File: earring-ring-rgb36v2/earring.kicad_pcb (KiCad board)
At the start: 2 copper layers, 75 x 92.5 mm, 65 parts, among them J1 Conn_01x05, Q1 AO3401A, Q2 Q_Photo_NPN_EC, SW1 SW_Push, U2 STM32L031G6Ux, Y1 Crystal

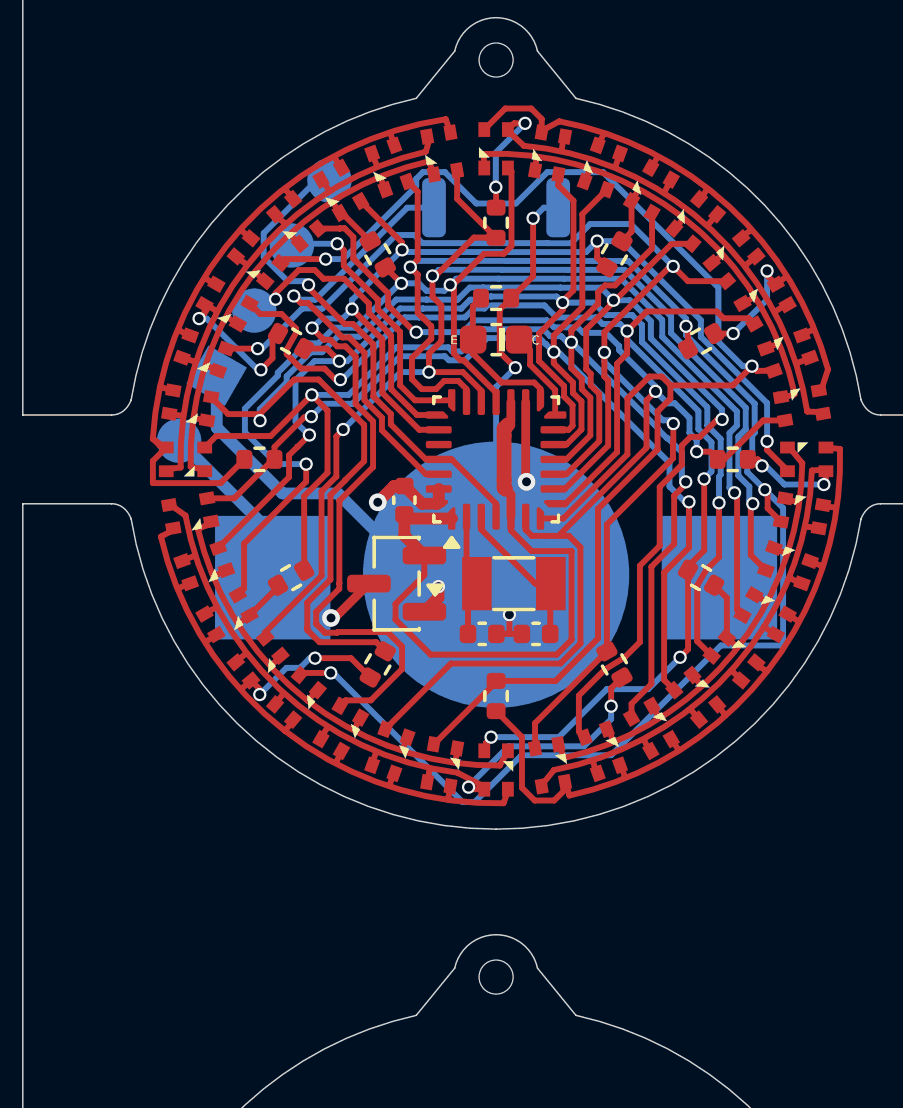
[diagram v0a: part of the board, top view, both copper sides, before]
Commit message: earring-ring-rgb36v2: add microphone
This also required reworking the PCB a little.
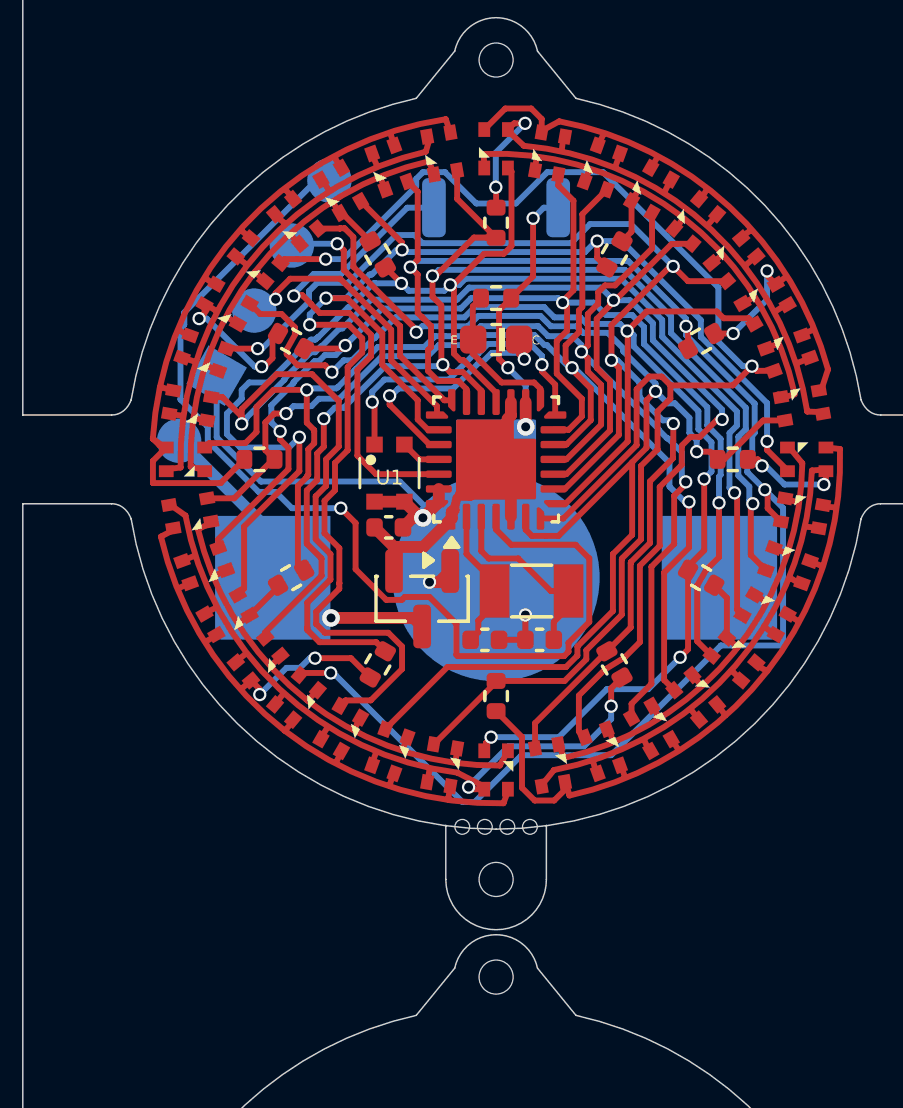
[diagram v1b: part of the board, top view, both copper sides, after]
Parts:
- added REF**: ToolingHoleWithMouseBytes, Custom:ToolingHoleWithMouseBytes, F.Cu at (0.00, 14.2)
- added U1: GMA2718H09-F42-4P, Custom:GMA2718H09-F42-4P, F.Cu at (-3.60, 0.47)
- moved C1 1.06 mm to (-3.63, 2.30), turned to 0 degrees
- moved Q1 1.00 mm to (-2.50, 4.71), turned to -90 degrees
- moved Y1 0.65 mm to (1.20, 4.45)
- moved C3 0.23 mm to (1.47, 6.10)
- moved C2 0.22 mm to (-0.38, 6.10)
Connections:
- U2 pad 14: PHOTO_VCC -> MIC_SENSE
- U2 pad 24: unconnected-(U2-PB3-Pad24) -> PHOTO_VCC
- U2 pad 25: NRST -> MIC_VCC
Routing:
- net NRST: track 16.8 -> 35.9 mm
- net VCC: track 22.4 -> 8.89 mm
- net MIC_SENSE: track 0.00 -> 10.6 mm, vias 0 -> 2
- net GND: track 43.2 -> 34.2 mm
- net PHOTO_VCC: track 3.05 -> 8.57 mm, vias 0 -> 2
- net A12: track 41.1 -> 44.1 mm
- net Net-(U2-PB7): track 14.7 -> 16.5 mm
- net A1: track 49.5 -> 51.3 mm
- net A4: track 47.5 -> 49.3 mm
- net VBAT: track 9.99 -> 11.5 mm
- net MIC_VCC: track 0.00 -> 1.37 mm
- net Net-(U2-PC15): track 5.25 -> 6.53 mm
- net A2: track 55.4 -> 54.3 mm
- net A6: track 38.9 -> 39.7 mm
- net A3: track 42.3 -> 43.1 mm
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
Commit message: earring-ring-rgb36v2: switch to 10k resistor for light sensing
Based on some very rough measurements and calculations, I think this
will end up as ~2V input voltage on the ADC on a bright 400 nits
display.

This is also the version that was sent to JLCPCB as a test production.
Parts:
- R13: value 1k -> 10k
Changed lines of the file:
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@@
 			)
 		)
-		(property "Value" "1k"
+		(property "Value" "10k"
 			(at 0 1.17 0)
 			(layer "F.Fab")
@@
 			)
 		)
-		(property "LCSC" "C11702"
+		(property "LCSC" "C25756"
 			(at 0 0 0)
 			(unlocked yes)

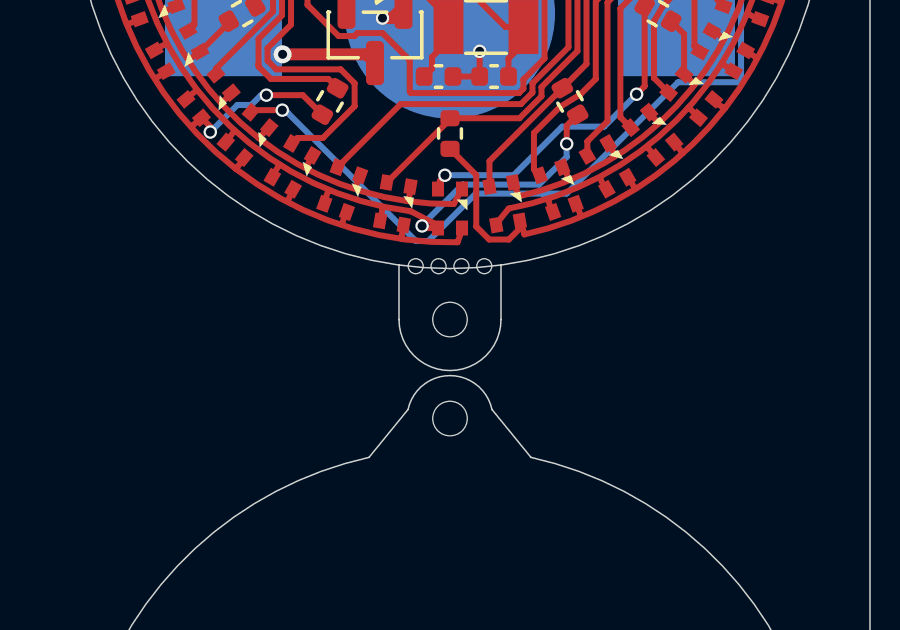
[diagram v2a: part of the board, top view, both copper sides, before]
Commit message: earring-ring-rgb36v2: add 3D model for the microphone
Also remove the tooling hole at the bottom, they were messing with the
3D view.
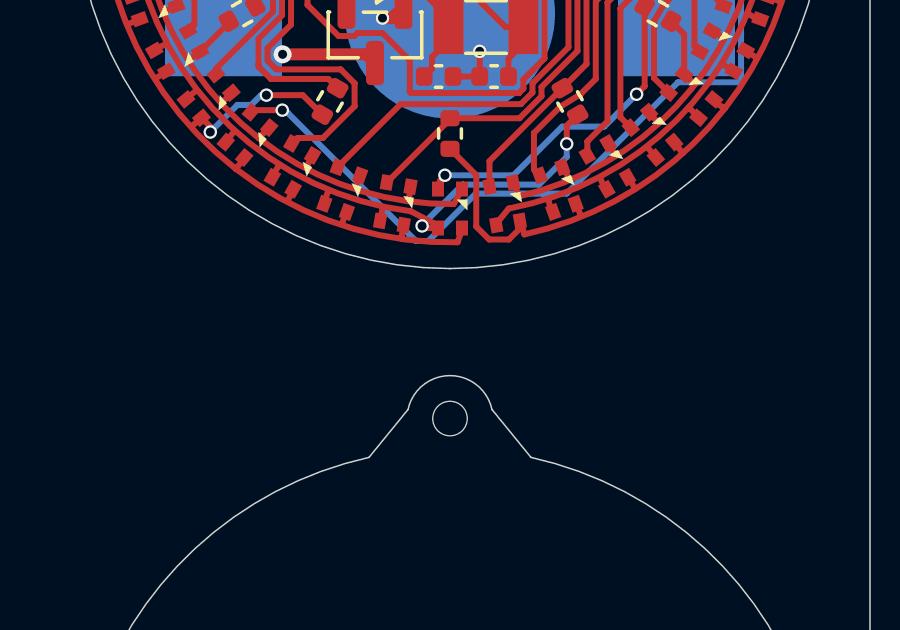
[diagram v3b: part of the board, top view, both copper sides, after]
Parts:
- removed REF**: ToolingHoleWithMouseBytes, Custom:ToolingHoleWithMouseBytes
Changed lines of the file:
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@@
 		)
 		(embedded_fonts no)
+		(model "../../../third_party/lcsc/C5142165.step"
+			(offset
+				(xyz 0 0 0.5)
+			)
+			(scale
+				(xyz 1 1 1)
+			)
+			(rotate
+				(xyz -0 -0 -0)
+			)
+		)
 	)
 	(footprint "Custom:NH-Z1415RGBA-SG"
@@
 		)
 	)
-	(footprint "Custom:ToolingHoleWithMouseBytes"
-		(layer "F.Cu")
-		(at 0 14.2)
-		(property "Reference" "REF**"
-			(at 0 -5.1 0)
-			(unlocked yes)
-			(layer "F.SilkS")
-			(hide yes)
-			(effects
-				(font
-					(size 1 1)
-					(thickness 0.1)
-				)
-			)
-		)
-		(property "Value" "ToolingHoleWithMouseBytes"
-			(at 0 -3.6 0)
-			(unlocked yes)
-			(layer "F.Fab")
-			(hide yes)
-			(effects
-				(font
-					(size 1 1)
-					(thickness 0.15)
-				)
-			)
-		)
-		(property "Datasheet" ""
-			(at 0 0 0)
-			(unlocked yes)
-			(layer "F.Fab")
-			(hide yes)
-			(effects
-				(font
-					(size 1 1)
-					(thickness 0.15)
-				)
-			)
-		)
-		(property "Description" ""
-			(at 0 0 0)
-			(unlocked yes)
-			(layer "F.Fab")
-			(hide yes)
-			(effects
-				(font
-					(size 1 1)
-					(thickness 0.15)
-				)
-			)
-		)
-		(attr through_hole board_only dnp)
-		(fp_line
-			(start -1.7 0)
-			(end -1.7 -1.83)
-			(stroke
-				(width 0.05)
-				(type default)
-			)
-			(layer "Edge.Cuts")
-		)
-		(fp_line
-			(start 1.7 0)
-			(end 1.7 -1.83)
-			(stroke
-				(width 0.05)
-				(type default)
-			)
-			(layer "Edge.Cuts")
-		)
-		(fp_arc
-			(start 1.7 0)
-			(mid 0 1.7)
-			(end -1.7 0)
-			(stroke
-				(width 0.05)
-				(type default)
-			)
-			(layer "Edge.Cuts")
-		)
-		(pad "" np_thru_hole circle
-			(at -1.143 -1.778)
-			(size 0.5 0.5)
-			(drill 0.5)
-			(layers "*.Mask")
-		)
-		(pad "" np_thru_hole circle
-			(at -0.381 -1.778)
-			(size 0.5 0.5)
-			(drill 0.5)
-			(layers "*.Mask")
-		)
-		(pad "" np_thru_hole circle
-			(at 0 0)
-			(size 1.152 1.152)
-			(drill 1.152)
-			(layers "*.Mask")
-			(solder_mask_margin 0.148)
-			(clearance 0.248)
-		)
-		(pad "" np_thru_hole circle
-			(at 0.381 -1.778)
-			(size 0.5 0.5)
-			(drill 0.5)
-			(layers "*.Mask")
-		)
-		(pad "" np_thru_hole circle
-			(at 1.143 -1.778)
-			(size 0.5 0.5)
-			(drill 0.5)
-			(layers "*.Mask")
-		)
-		(embedded_fonts no)
-	)
 	(footprint "Custom:NH-Z1415RGBA-SG"
